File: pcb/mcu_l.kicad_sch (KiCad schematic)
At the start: 30 parts, among them J1 USB_C_Receptacle_USB2.0_16P, SW1 BOOTSEL, SW2 RESET, U1 W25Q128JVS, U2 RP2040, U3 AMS1117-3.3, Y1 ABM8-272-T3

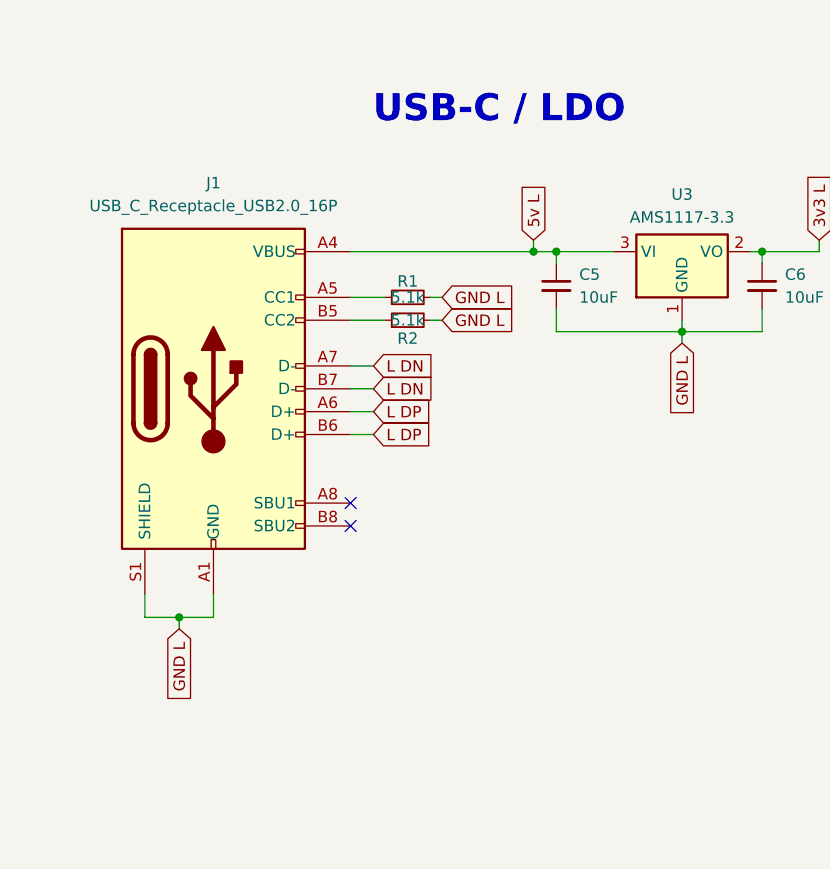
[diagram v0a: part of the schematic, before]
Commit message: Initial PCB v1.1.0 updates, including 4-layer restructure
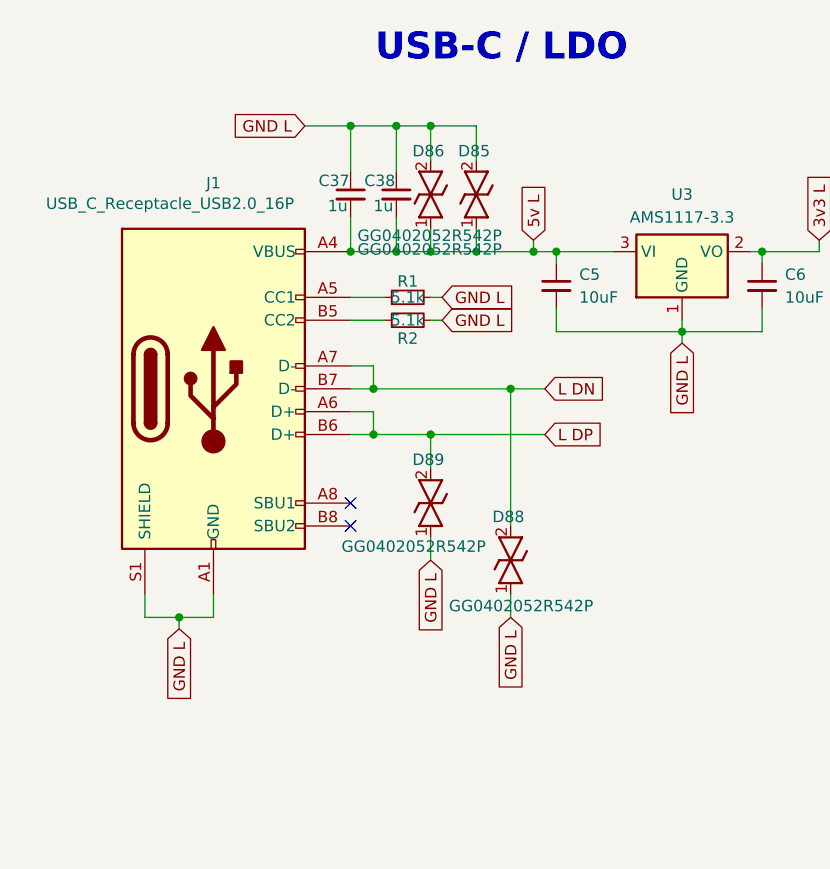
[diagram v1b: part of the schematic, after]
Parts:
- added C37, C38: 1u, Capacitor_SMD:C_0603_1608Metric, symbol Device:C_Small
- added D85, D86, D88, D89: GG0402052R542P, GG0402052R542P:DIONC1006X55N, symbol GG0402052R542P:GG0402052R542P
- SW1, SW2: footprint Button_Switch_SMD:SW_SPST_EVQP0 -> EVQ-P9P02W:EVQ-P9P02W
- U1: footprint Package_SO:SOIC-8_5.23x5.23mm_P1.27mm -> W25Q128JVSIQ:SOIC127P790X216-8N
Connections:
- net 5v L: now also C37.2, C38.2, D85.1, D86.1
- net GND L: now also C37.1, C38.1, D85.2, D86.2, D88.1, D89.1
- net L DN: now also D88.2
- net L DP: now also D89.2

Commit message: Include components as a path in the repository
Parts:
- SW1, SW2: footprint EVQ-P9P02W:EVQ-P9P02W -> EVQ-P9P02W:EVQP2202M
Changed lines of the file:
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@@
 			)
 		)
-		(property "Footprint" "EVQ-P9P02W:EVQ-P9P02W"
+		(property "Footprint" "EVQ-P9P02W:EVQP2202M"
 			(at 195.58 60.96 0)
 			(hide yes)
@@
 			)
 		)
-		(property "Footprint" "EVQ-P9P02W:EVQ-P9P02W"
+		(property "Footprint" "EVQ-P9P02W:EVQP2202M"
 			(at 151.13 157.48 0)
 			(hide yes)
